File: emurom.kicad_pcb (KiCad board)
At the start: 2 copper layers, 90.6 x 77.8 mm, 58 parts, among them J1 AVR-ISP, J2 USB_B_Micro, J3 idc2k, J4 dip2k, J5 idc32k, J6 dip32k, J7 SYSRST, U1 ATmega328P-AU, U10 conn2k, U11 conn32k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

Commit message: renamed to emurom
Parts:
- G***: footprint romdev:gnulogo -> emurom:gnulogo
- J3, U10: footprint romdev:conn2k -> emurom:conn2k
- J5, U11: footprint romdev:conn32k -> emurom:conn32k
- mouse-bite-2mm-slot (x5): footprint romdev:mouse-bite-2mm-slot -> emurom:mouse-bite-2mm-slot
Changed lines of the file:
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@@
     (add_net VCC)
   )
-  (module romdev:gnulogo (layer F.Cu)
+  (module emurom:gnulogo (layer F.Cu)
     (at 170.4 70)
     (fp_text reference G*** (at 0.1 9.3) (layer F.SilkS) hide
@@
       (xy -0.017575 -3.712307) (xy 0 -3.712308) (xy 0.139878 -3.712224)) (layer F.SilkS) (width 0.01))
   )
-  (module romdev:mouse-bite-2mm-slot (layer F.Cu)
+  (module emurom:mouse-bite-2mm-slot (layer F.Cu)
     (at 195.8 91.2 90)
     (fp_text reference mouse-bite-2mm-slot (at 0 -2 90) (layer F.SilkS) hide
@@
     (pad "" np_thru_hole circle (at 0 -0.75 90) (size 0.5 0.5) (drill 0.5) (layers *.Cu *.Mask))
   )
-  (module romdev:mouse-bite-2mm-slot (layer F.Cu)
+  (module emurom:mouse-bite-2mm-slot (layer F.Cu)
     (at 230.4 77)
     (fp_text reference mouse-bite-2mm-slot (at 0 -2) (layer F.SilkS) hide
@@
     (pad "" np_thru_hole circle (at 0.75 0.75) (size 0.5 0.5) (drill 0.5) (layers *.Cu *.Mask))
   )
-  (module romdev:mouse-bite-2mm-slot (layer F.Cu)
+  (module emurom:mouse-bite-2mm-slot (layer F.Cu)
     (at 205.1 77)
     (fp_text reference mouse-bite-2mm-slot (at 0 -2) (layer F.SilkS) hide
@@
     (pad "" np_thru_hole circle (at 0 -0.75) (size 0.5 0.5) (drill 0.5) (layers *.Cu *.Mask))
   )
-  (module romdev:mouse-bite-2mm-slot (layer F.Cu)
+  (module emurom:mouse-bite-2mm-slot (layer F.Cu)
     (at 189.1 77)
     (fp_text reference mouse-bite-2mm-slot (at 0 -2) (layer F.SilkS) hide
@@
     (pad "" np_thru_hole circle (at 0.75 0.75) (size 0.5 0.5) (drill 0.5) (layers *.Cu *.Mask))
   )
-  (module romdev:mouse-bite-2mm-slot (layer F.Cu)
+  (module emurom:mouse-bite-2mm-slot (layer F.Cu)
     (at 166.3 77)
     (fp_text reference mouse-bite-2mm-slot (at 0 -2) (layer F.SilkS) hide
@@
     )
   )
-  (module romdev:conn2k (layer F.Cu)
+  (module emurom:conn2k (layer F.Cu)
     (at 163.73 89.916 90)
     (descr "Through hole straight pin header, 2x12, 2.54mm pitch, double rows")
@@
     )
   )
-  (module romdev:conn32k (layer F.Cu)
+  (module emurom:conn32k (layer F.Cu)
     (at 233.014 87.284 270)
     (descr "Through hole straight pin header, 2x14, 2.54mm pitch, double rows")
@@
     )
   )
-  (module romdev:conn2k (layer F.Cu)
+  (module emurom:conn2k (layer F.Cu)
     (at 228.6 37.338)
     (descr "Through hole straight pin header, 2x12, 2.54mm pitch, double rows")
@@
     )
   )
-  (module romdev:conn32k (layer F.Cu)
+  (module emurom:conn32k (layer F.Cu)
     (at 239.014 32.258)
     (descr "Through hole straight pin header, 2x14, 2.54mm pitch, double rows")

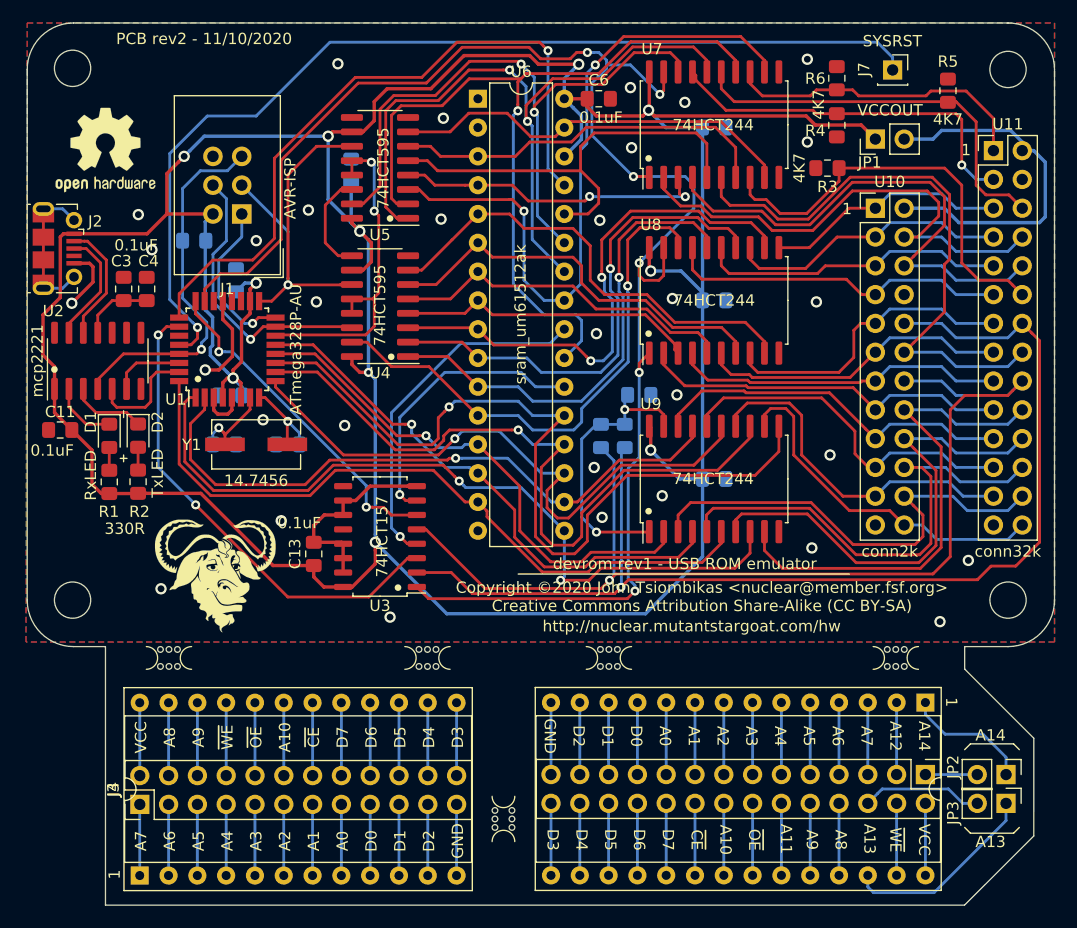
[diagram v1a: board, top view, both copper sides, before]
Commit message: - attempt to fix issue #1 about the address jumpers being too close to   the IDC connector. - added BOM and release links to the README
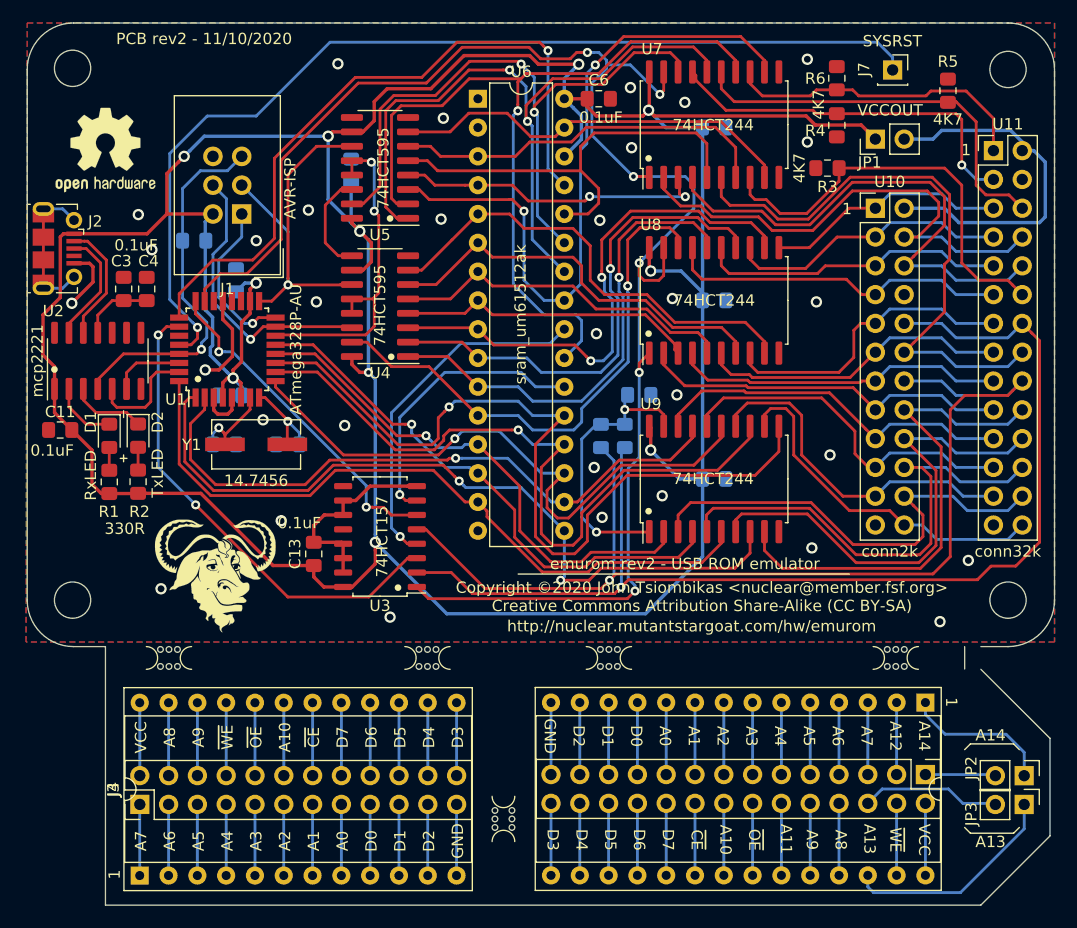
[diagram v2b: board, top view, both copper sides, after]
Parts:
- moved JP3 1.60 mm to (241.7, 89.9)
- moved JP2 1.60 mm to (241.7, 87.4)
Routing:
- net /dipconn/rom32k-1: track 11.3 -> 13.2 mm
- net /dipconn/rom32k-26: track 17.6 -> 19.5 mm
- net Net-(J5-Pad26): track 10.7 -> 12.3 mm
- net Net-(J5-Pad1): track 4.57 -> 6.21 mm
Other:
- outline, holes or cut-outs redrawn
- board text added: "emurom rev2 - USB ROM emulator"
- board text added: "http://nuclear.mutantstargoat.com/hw/emurom"
- board text removed: "devrom rev1 - USB ROM emulator"
- board text removed: "http://nuclear.mutantstargoat.com/hw"

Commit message: version update
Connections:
- net /~CS renamed /~{CS}
- net /~OE renamed /~{OE}
- net /~RAMCS renamed /~{RAMCS}
- net /~RAMOE renamed /~{RAMOE}
- net /~RST renamed /~{RST}
- net /~SS renamed /~{SS}
- net /~SYSCS renamed /~{SYSCS}
- net /~SYSOE renamed /~{SYSOE}
- net /~SYSRST renamed /~{SYSRST}
- net /~WR renamed /~{WR}
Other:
- net class Default removed
- net class power removed
- board text added: "~{CE}"
- board text added: "~{OE}"
- board text added: "~{WE}"
- board text removed: "~CE"
- board text removed: "~OE"
- board text removed: "~WE"
